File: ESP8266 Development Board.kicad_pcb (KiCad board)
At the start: 2 copper layers, 75.6 x 53.6 mm, 21 parts, among them J1 Barrel_Jack, J2 Conn_01x01_Female, J3 Conn_01x01_Female, SW1 SW_SPST, SW2 SW_Push, U1 ESP8266-12E_Dev_Board

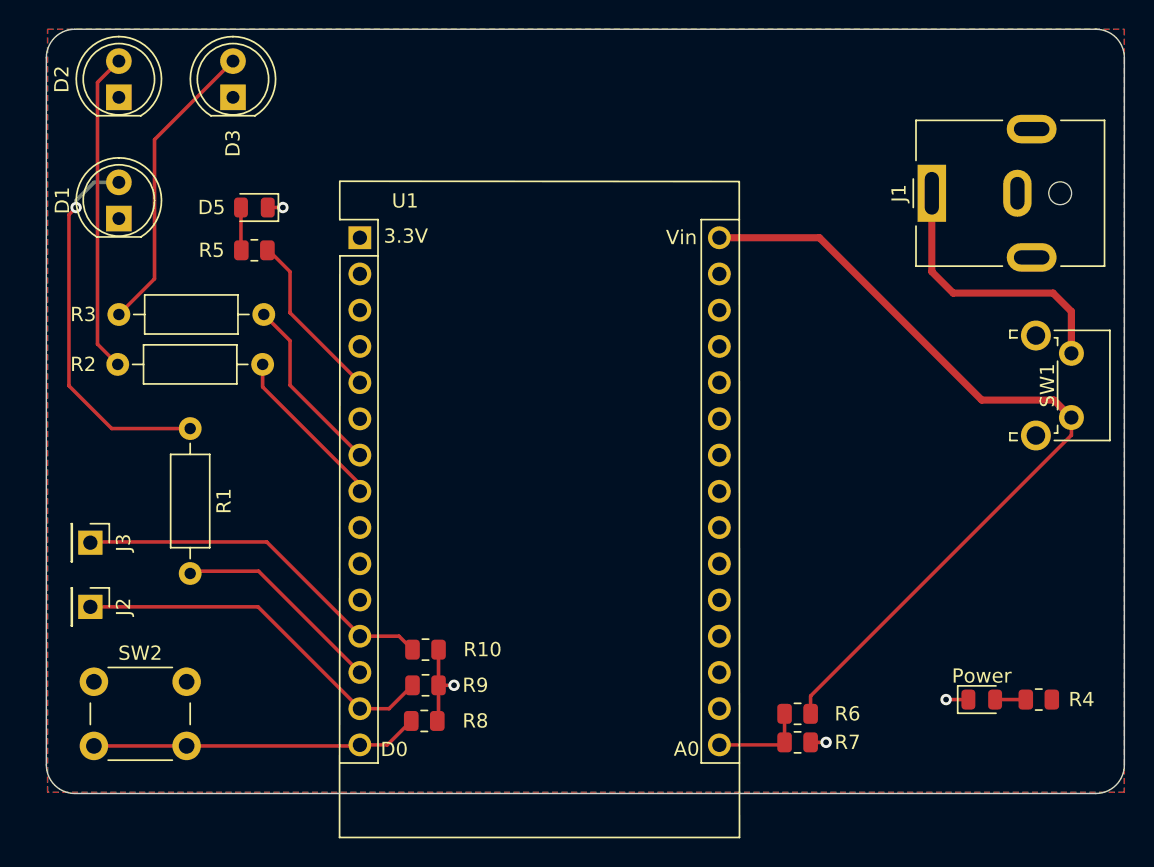
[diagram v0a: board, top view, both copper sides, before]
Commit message: Updated footprint to better guess; STILL NOT VERIFIED
Got a picture with some measurements and updated the ESP8266-12E footprint.
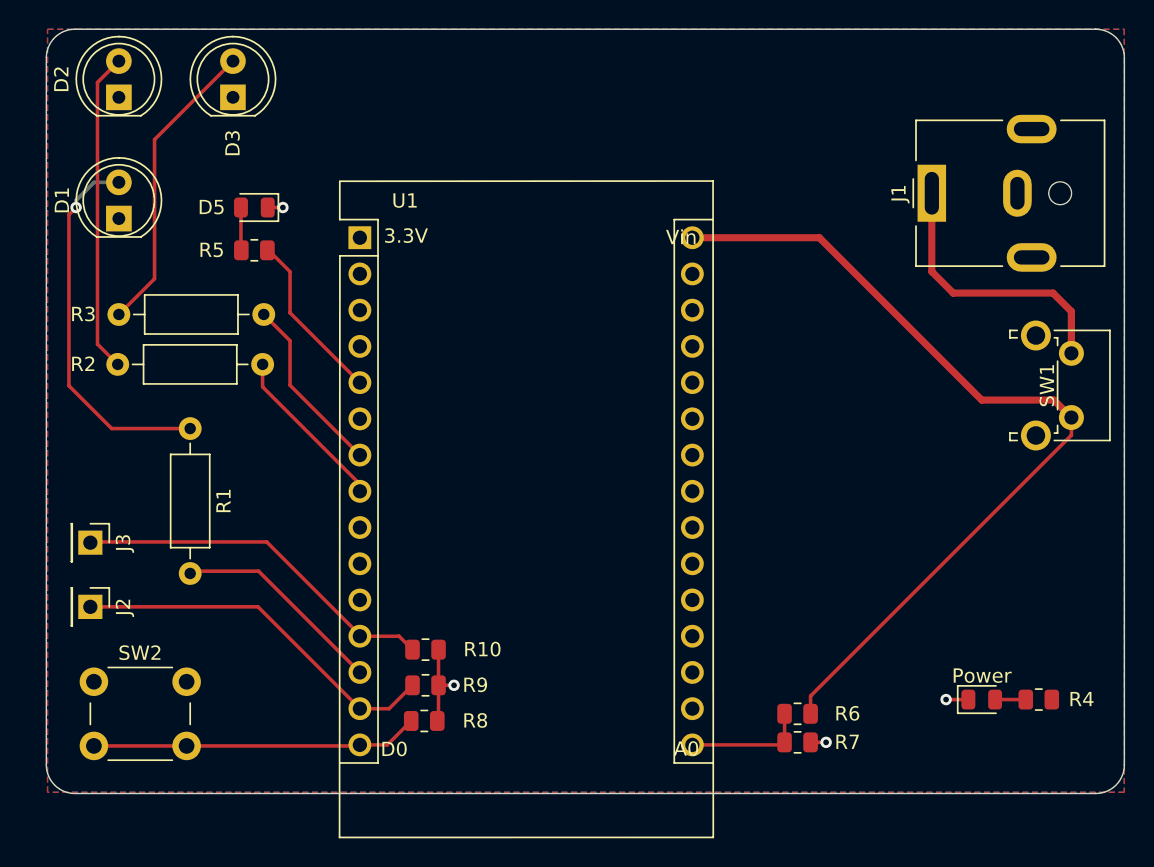
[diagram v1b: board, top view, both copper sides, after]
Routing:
- net /Vin: track 58.3 -> 60.1 mm
- net /A0: track 6.39 -> 8.29 mm

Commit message: Added JST headers
Added JST headers with ground points and cool 3D models
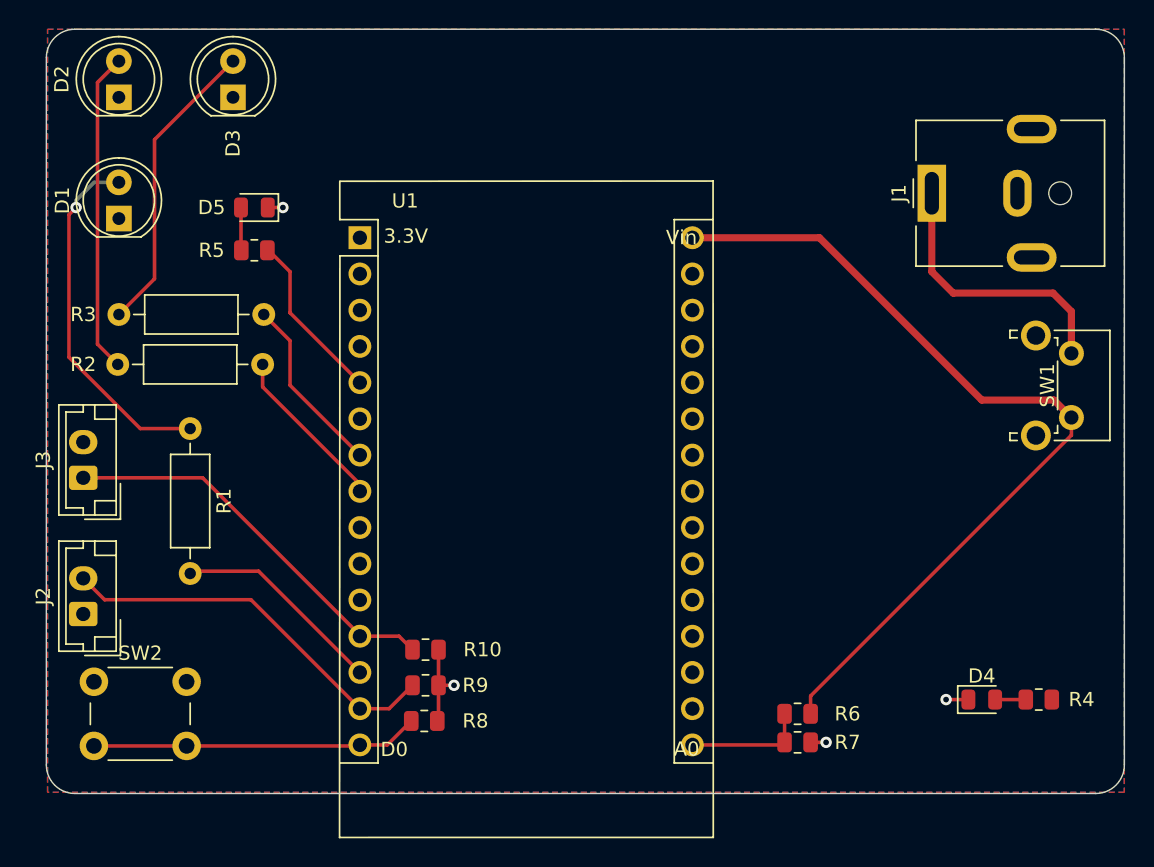
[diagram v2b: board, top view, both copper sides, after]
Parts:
- J2, J3: value Conn_01x01_Female -> Conn_01x02_Female; footprint Connector_PinHeader_2.54mm:PinHeader_1x01_P2.54mm_Vertical -> Connector_JST:JST_EH_B2B-EH-A_1x02_P2.50mm_Vertical
- moved J3 4.58 mm to (107.5, 83.0), turned to 90 degrees
- moved J2 0.71 mm to (107.5, 92.5), turned to 90 degrees
- renumbered Power to D4
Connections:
- J2 pad 1: /D1 -> GND
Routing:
- net /D3: track 25.8 -> 28.1 mm
- net /D1: track 26.2 -> 27.6 mm
- net Net-(D1-Pad2): track 26.5 -> 25.3 mm
